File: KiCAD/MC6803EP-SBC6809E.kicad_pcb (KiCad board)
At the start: 2 copper layers, 57 x 60 mm, 5 parts, among them U1 MC6809E ソケット, U2 74HCT02, U3 MC6800

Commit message: REV1 ガーバーデータ出力
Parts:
- added C1: 0.1u, Capacitor_THT:C_Disc_D3.0mm_W1.6mm_P2.50mm, F.Cu at (138.1, 94.4)
- added J1: I/O PIN, Connector_PinHeader_2.54mm:PinHeader_1x08_P2.54mm_Horizontal, F.Cu at (146.5, 124.9)
- added J2: CONT PIN, Connector_PinHeader_2.54mm:PinHeader_1x05_P2.54mm_Horizontal, F.Cu at (161.6, 125.0)
- added J3: SBC68_BUS, Connector_PinHeader_2.54mm:PinHeader_2x20_P2.54mm_Horizontal, F.Cu at (162.3, 73.4)
- added R1: 10k, Resistor_THT:R_Axial_DIN0207_L6.3mm_D2.5mm_P10.16mm_Horizontal, F.Cu at (152.2, 86.6)
- added R2: 10k, Resistor_THT:R_Axial_DIN0207_L6.3mm_D2.5mm_P10.16mm_Horizontal, F.Cu at (151.9, 100.0)
- added R3: 10k, Resistor_THT:R_Axial_DIN0207_L6.3mm_D2.5mm_P10.16mm_Horizontal, F.Cu at (146.5, 99.9)
- added U4: 74LS573, Package_DIP:DIP-20_W7.62mm_Socket, F.Cu at (129.9, 97.4)
- U1: footprint Package_DIP:DIP-40_W15.24mm_Socket_LongPads -> Package_DIP:DIP-40_W15.24mm_Socket
- U2: footprint Package_DIP:DIP-14_W7.62mm_Socket_LongPads -> Package_DIP:DIP-14_W7.62mm_Socket
- U3: value MC6800 -> MC6803EP; footprint Package_DIP:DIP-40_W15.24mm_Socket_LongPads -> Package_DIP:DIP-40_W15.24mm_Socket
- moved C3 8.48 mm to (146.2, 88.2), turned to 0 degrees
- moved U1 1.98 mm to (109.5, 73.2)
- moved C2 1.61 mm to (137.8, 72.2)
- moved U2 1.40 mm to (129.8, 75.2)
- moved U3 1.17 mm to (141.9, 73.1)
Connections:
- U3 pad 10: /A1 -> Net-(J2-Pad3)
- U3 pad 11: /A2 -> Net-(J2-Pad4)
- U3 pad 12: /A3 -> Net-(J2-Pad5)
- U3 pad 13: /A4 -> Net-(J1-Pad1)
- U3 pad 14: /A5 -> Net-(J1-Pad2)
- U3 pad 15: /A6 -> Net-(J1-Pad3)
- U3 pad 16: /A7 -> Net-(J1-Pad4)
- U3 pad 17: /A8 -> Net-(J1-Pad5)
- U3 pad 18: /A9 -> Net-(J1-Pad6)
- U3 pad 19: /A10 -> Net-(J1-Pad7)
- U3 pad 20: /A11 -> Net-(J1-Pad8)
- U3 pad 21: GND -> VCC
- U3 pad 22: /A12 -> /A15
- U3 pad 23: /A13 -> /A14
- U3 pad 24: /A14 -> /A13
- U3 pad 25: /A15 -> /A12
- U3 pad 26: /D7 -> /A11
- U3 pad 27: /D6 -> /A10
- U3 pad 28: /D5 -> /A9
- U3 pad 29: /D4 -> /A8
- U3 pad 3: /PHI1 -> unconnected-(U3-Pad3)
- U3 pad 30: /D3 -> /D7
- U3 pad 31: /D2 -> /D6
- U3 pad 32: /D1 -> /D5
- U3 pad 33: /D0 -> /D4
- U3 pad 34: /R/~{W} -> /D3
- U3 pad 35: unconnected-(U3-Pad35) -> /D2
- U3 pad 36: /PHI2 -> /D1
- U3 pad 37: /PHI2 -> /D0
- U3 pad 38: unconnected-(U3-Pad38) -> /R/~{W}
- U3 pad 39: /TSC -> /PHI1
- U3 pad 4: /~{IRQ} -> /~{NMI}
- U3 pad 40: /~{RES} -> /PHI2
- U3 pad 5: unconnected-(U3-Pad5) -> /~{IRQ}
- U3 pad 6: /~{NMI} -> /~{RES}
- U3 pad 7: unconnected-(U3-Pad7) -> VCC
- U3 pad 8: VCC -> Net-(J2-Pad1)
- U3 pad 9: /A0 -> Net-(J2-Pad2)
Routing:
- net /PHI1: track 24.6 -> 150.7 mm
- net /A4: track 32.2 -> 146.6 mm, vias 0 -> 2
- net /A5: track 32.2 -> 144.1 mm, vias 0 -> 1
- net /A3: track 33.1 -> 126.8 mm, vias 0 -> 1
- net /D3: track 33.3 -> 126.2 mm, vias 0 -> 2
- net /D5: track 33.3 -> 124.8 mm, vias 0 -> 1
- net /A8: track 32.2 -> 117.2 mm, vias 0 -> 2
- net /A11: track 32.2 -> 110.5 mm, vias 0 -> 2
- net /D4: track 33.3 -> 111.3 mm, vias 0 -> 1
- net /A10: track 32.2 -> 108.5 mm, vias 0 -> 1
- net /A9: track 32.2 -> 106.3 mm, vias 0 -> 1
- net /A7: track 32.2 -> 105.3 mm
- net /D6: track 33.3 -> 105.6 mm, vias 0 -> 1
- net VCC: track 55.4 -> 127.0 mm, vias 0 -> 1
- net Net-(J2-Pad2): track 0.00 -> 65.1 mm
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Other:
- board size 57 x 60 mm -> 70 x 63 mm
- board text added: "10"
- board text added: "11"
- board text added: "12"
- board text added: "13"
- board text added: "14"
- board text added: "15"
- board text added: "16"
- board text added: "17"
- board text added: "20"
- board text added: "21"
- board text added: "22"
- board text added: "23"
- board text added: "24"
- board text added: "74HCT573"
- board text added: "MC6803EP MPU"
- board text added: "MC6803EP for SBC6809E KUNI-NET 2022"
- board text removed: "MC6800 MPU"
- board text removed: "MC6800 for SBC6809E KUNI-NET 2022"

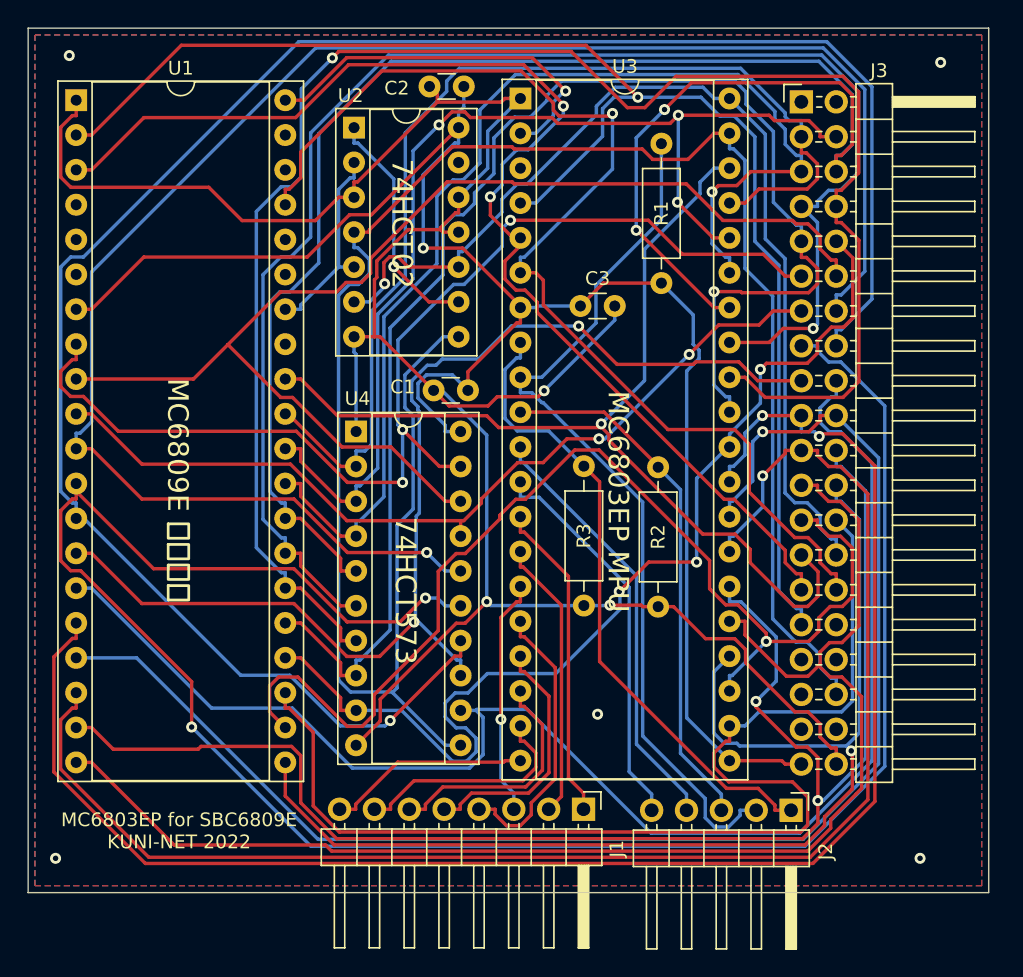
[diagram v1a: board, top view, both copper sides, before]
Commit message: REV1 回路変更(シリアル端子)、ガーバー再出力
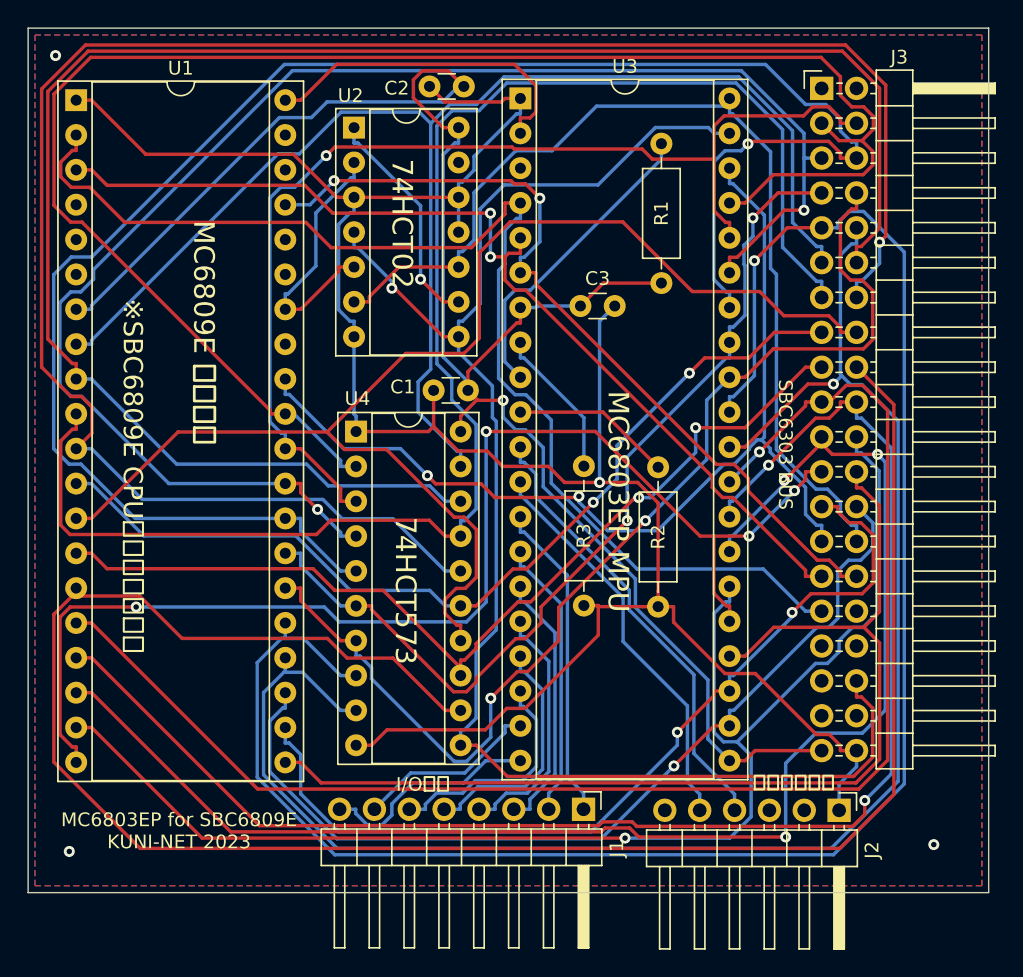
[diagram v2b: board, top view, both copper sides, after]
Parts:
- J2: value CONT PIN -> SERIAL Con; footprint Connector_PinHeader_2.54mm:PinHeader_1x05_P2.54mm_Horizontal -> Connector_PinHeader_2.54mm:PinHeader_1x06_P2.54mm_Horizontal
- moved J2 3.50 mm to (165.1, 125.0)
- moved J3 1.78 mm to (163.8, 72.4)
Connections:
- J2 pad 1: Net-(J2-Pad1) -> GND
- J2 pad 2: Net-(J2-Pad2) -> unconnected-(J2-Pin_2-Pad2)
- J2 pad 3: Net-(J2-Pad3) -> unconnected-(J2-Pin_3-Pad3)
- R1 pad 2: Net-(J2-Pad2) -> Net-(U3-T-OUT-P21)
- R2 pad 1: Net-(J2-Pad3) -> Net-(U3-SCLK-P22)
- R3 pad 1: Net-(J2-Pad1) -> Net-(U3-TIN-P20)
- U3 pad 10: Net-(J2-Pad3) -> Net-(U3-SCLK-P22)
- U3 pad 8: Net-(J2-Pad1) -> Net-(U3-TIN-P20)
- U3 pad 9: Net-(J2-Pad2) -> Net-(U3-T-OUT-P21)
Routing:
- net /A4: track 146.6 -> 67.7 mm
- net Net-(J2-Pad2): track 65.1 -> 0.00 mm
- net /A2: track 63.7 -> 112.3 mm, vias 2 -> 0
- net /A5: track 144.1 -> 96.9 mm, vias 1 -> 0
- net Net-(J2-Pad1): track 46.7 -> 0.00 mm
- net /D5: track 124.8 -> 80.9 mm, vias 1 -> 2
- net /D4: track 111.3 -> 67.8 mm, vias 1 -> 2
- net /D0: track 78.0 -> 121.1 mm
- net /D7: track 77.1 -> 119.6 mm, vias 3 -> 1
- net /A1: track 87.8 -> 130.2 mm
- net Net-(J2-Pad3): track 38.7 -> 0.00 mm
- net /PHI1: track 150.7 -> 112.6 mm, vias 0 -> 1
- net /A7: track 105.3 -> 142.7 mm
- net /D6: track 105.6 -> 134.7 mm
- net /D2: track 85.4 -> 111.1 mm, vias 1 -> 2
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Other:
- board text added: "I/O端子"
- board text added: "MC6803EP for SBC6809E KUNI-NET 2023"
- board text added: "SBC6303 BUS"
- board text added: "※SBC6809E CPUソケット接続用"
- board text added: "シリアル端子"
- board text removed: "20"
- board text removed: "21"
- board text removed: "22"
- board text removed: "23"
- board text removed: "24"
- board text removed: "MC6803EP for SBC6809E KUNI-NET 2022"
